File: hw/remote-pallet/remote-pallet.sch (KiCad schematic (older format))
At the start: 25 parts, among them J1 Power, M0 E-MATCH, M1 E-MATCH, M2 E-MATCH, M3 E-MATCH, M4 E-MATCH, M5 E-MATCH, M6 E-MATCH, M7 E-MATCH, Q1 EMatch Test, SW1 Power, SW2 Arm Hardware, U1 Photon Power, U2 PHOTON, U3 Armed Sense

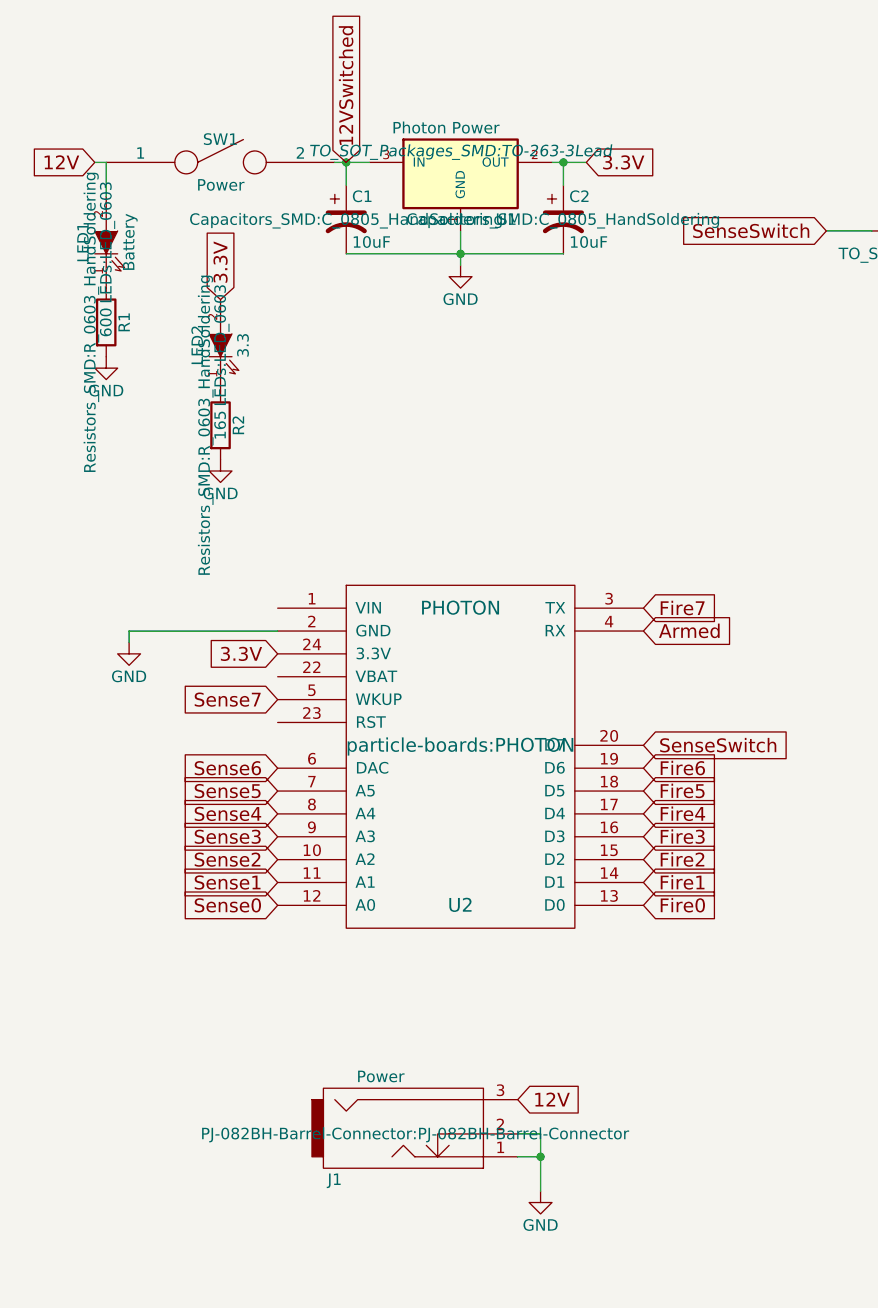
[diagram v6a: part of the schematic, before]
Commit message: updating pcb and adding part numbers for digikey
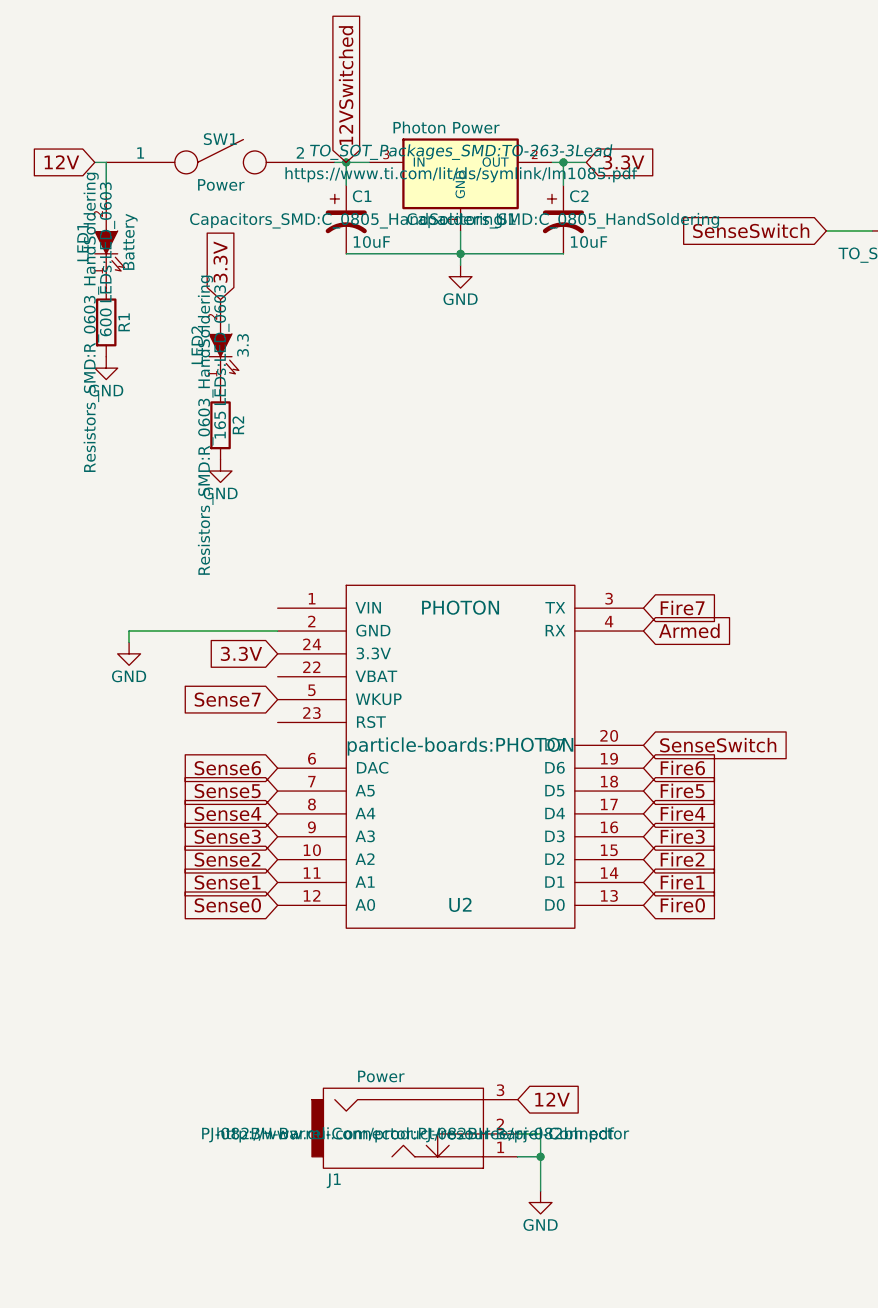
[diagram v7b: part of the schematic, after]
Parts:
- C1, C2: digikey part no (none) -> 511-1683-1-ND
- C3: digikey part no (none) -> 587-1290-1-ND
- C4: digikey part no (none) -> 490-5523-1-ND
- J1: digikey part no (none) -> CP-082BHCT-ND; mates with (none) -> CP3-002BH-ND
- LED1: digikey part no (none) -> 732-4978-1-ND
- LED2: digikey part no (none) -> 732-4981-1-ND
- LED3: digikey part no (none) -> 732-4971-1-ND
- M0, M1, M2, M3, M4, M5, M6, M7: digikey part no (none) -> ED2740-ND
- Q1: digikey part no (none) -> BSS84PH6433XTMA1CT-ND
- R1, R3: digikey part no (none) -> 311-600HCT-ND
- R2: digikey part no (none) -> 311-165HRCT-ND
- SW1, SW2: digikey part no (none) -> 360-3287-ND
- U1: digikey part no (none) -> LM1085ISX-3.3/NOPBCT-ND
- U3: digikey part no (none) -> TA48S033AF(T6L1Q)CT-ND
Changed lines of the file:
@@
 F 1 "Photon Power" H 2050 1200 50  0000 L CNN
 F 2 "TO_SOT_Packages_SMD:TO-263-3Lead" H 2350 1100 50  0000 C CIN
-F 3 "" H 2350 1000 50  0000 C CNN
+F 3 "https://www.ti.com/lit/ds/symlink/lm1085.pdf" H 2350 1000 50  0000 C CNN
+F 4 "LM1085ISX-3.3/NOPBCT-ND" H 2350 1000 60  0001 C CNN "digikey part no"
 	1    2350 1000
 	1    0    0    -1
@@
 F 2 "M2011LL1W01-switch:M2011LL1W01" H 9250 1250 50  0001 C CNN
 F 3 "" H 9250 1250 50  0000 C CNN
+F 4 "360-3287-ND" H 9250 1250 60  0001 C CNN "digikey part no"
 	1    9250 1250
 	1    0    0    -1
@@
 F 2 "TO_SOT_Packages_SMD:SOT-23" H 4550 1350 50  0000 C CNN
 F 3 "" H 4350 1250 50  0000 C CNN
+F 4 "BSS84PH6433XTMA1CT-ND" H 4350 1250 60  0001 C CNN "digikey part no"
 	1    4350 1250
 	1    0    0    1
@@
 F 2 "M2011LL1W01-switch:M2011LL1W01" H 1300 950 50  0001 C CNN
 F 3 "" H 1300 950 50  0000 C CNN
+F 4 "360-3287-ND" H 1300 950 60  0001 C CNN "digikey part no"
 	1    1300 950
 	1    0    0    -1
@@
 F 3 "" H 1850 1200 50  0000 C CNN
 F 4 "tantalum" H 1850 1200 60  0001 C CNN "type"
+F 5 "511-1683-1-ND" H 1850 1200 60  0001 C CNN "digikey part no"
 	1    1850 1200
 	1    0    0    -1
@@
 F 3 "" H 2800 1200 50  0000 C CNN
 F 4 "tantalum" H 2800 1200 60  0001 C CNN "type"
+F 5 "511-1683-1-ND" H 2800 1200 60  0001 C CNN "digikey part no"
 	1    2800 1200
 	1    0    0    -1
@@
 F 3 "" H 5700 1000 50  0000 C CNN
 F 4 "low-esr ceramic" H 5700 1000 60  0001 C CNN "type"
+F 5 "587-1290-1-ND" H 5700 1000 60  0001 C CNN "digikey part no"
 	1    5700 1000
 	1    0    0    -1
@@
 F 3 "" H 6750 1050 50  0000 C CNN
 F 4 "low-esr ceramic" H 6750 1050 60  0001 C CNN "type"
+F 5 "490-5523-1-ND" H 6750 1050 60  0001 C CNN "digikey part no"
 	1    6750 1050
 	1    0    0    -1
@@
 F 2 "Terminal_Blocks:TerminalBlock_Pheonix_PT-3.5mm_2pol" H 7050 2500 50  0001 C CNN
 F 3 "" H 7050 2500 50  0000 C CNN
+F 4 "ED2740-ND" H 7050 2500 60  0001 C CNN "digikey part no"
 	1    7050 2500
 	0    1    1    0
@@
 F 2 "Terminal_Blocks:TerminalBlock_Pheonix_PT-3.5mm_2pol" H 7050 3550 50  0001 C CNN
 F 3 "" H 7050 3550 50  0000 C CNN
+F 4 "ED2740-ND" H 7050 3550 60  0001 C CNN "digikey part no"
 	1    7050 3550
 	0    1    1    0
@@
 F 2 "Terminal_Blocks:TerminalBlock_Pheonix_PT-3.5mm_2pol" H 7050 4450 50  0001 C CNN
 F 3 "" H 7050 4450 50  0000 C CNN
+F 4 "ED2740-ND" H 7050 4450 60  0001 C CNN "digikey part no"
 	1    7050 4450
 	0    1    1    0
@@
 F 2 "Terminal_Blocks:TerminalBlock_Pheonix_PT-3.5mm_2pol" H 7050 5450 50  0001 C CNN
 F 3 "" H 7050 5450 50  0000 C CNN
+F 4 "ED2740-ND" H 7050 5450 60  0001 C CNN "digikey part no"
 	1    7050 5450
 	0    1    1    0
@@
 F 2 "Terminal_Blocks:TerminalBlock_Pheonix_PT-3.5mm_2pol" H 10050 2500 50  0001 C CNN
 F 3 "" H 10050 2500 50  0000 C CNN
+F 4 "ED2740-ND" H 10050 2500 60  0001 C CNN "digikey part no"
 	1    10050 2500
 	0    1    1    0
@@
 F 2 "Terminal_Blocks:TerminalBlock_Pheonix_PT-3.5mm_2pol" H 10050 3550 50  0001 C CNN
 F 3 "" H 10050 3550 50  0000 C CNN
+F 4 "ED2740-ND" H 10050 3550 60  0001 C CNN "digikey part no"
 	1    10050 3550
 	0    1    1    0
@@
 F 2 "Terminal_Blocks:TerminalBlock_Pheonix_PT-3.5mm_2pol" H 10050 4450 50  0001 C CNN
 F 3 "" H 10050 4450 50  0000 C CNN
+F 4 "ED2740-ND" H 10050 4450 60  0001 C CNN "digikey part no"
 	1    10050 4450
 	0    1    1    0
@@
 F 2 "Terminal_Blocks:TerminalBlock_Pheonix_PT-3.5mm_2pol" H 10050 5500 50  0001 C CNN
 F 3 "" H 10050 5500 50  0000 C CNN
+F 4 "ED2740-ND" H 10050 5500 60  0001 C CNN "digikey part no"
 	1    10050 5500
 	0    1    1    0
@@
 F 1 "Power" H 2000 5450 50  0000 C CNN
 F 2 "PJ-082BH-Barrel-Connector:PJ-082BH-Barrel-Connector" H 2150 5200 50  0000 C CNN
-F 3 "" H 2150 5200 50  0000 C CNN
+F 3 "http://www.cui.com/product/resource/pj-082bh.pdf" H 2150 5200 50  0000 C CNN
+F 4 "CP-082BHCT-ND" H 2150 5200 60  0001 C CNN "digikey part no"
+F 5 "CP3-002BH-ND" H 2150 5200 60  0001 C CNN "mates with"
 	1    2150 5200
 	1    0    0    -1
@@
 F 2 "TO_SOT_Packages_SMD:SOT-23-5" H 6250 850 50  0000 C CIN
 F 3 "http://ww1.microchip.com/downloads/en/DeviceDoc/MIC94310.pdf" H 6250 750 50  0000 C CNN
+F 4 "TA48S033AF(T6L1Q)CT-ND" H 6250 750 60  0001 C CNN "digikey part no"
 	1    6250 750
 	-1   0    0    -1
@@
 F 2 "LEDs:LED_0603" H 800 1300 50  0000 C CNN
 F 3 "" H 800 1300 50  0000 C CNN
+F 4 "732-4978-1-ND" H 800 1300 60  0001 C CNN "digikey part no"
 	1    800  1300
 	0    -1   -1   0
@@
 F 2 "LEDs:LED_0603" H 1300 1750 50  0000 C CNN
 F 3 "" H 1300 1750 50  0000 C CNN
+F 4 "732-4981-1-ND" H 1300 1750 60  0001 C CNN "digikey part no"
 	1    1300 1750
 	0    -1   -1   0
@@
 F 2 "LEDs:LED_0603" H 10400 1850 50  0000 C CNN
 F 3 "" H 10400 1850 50  0000 C CNN
+F 4 "732-4971-1-ND" H 10400 1850 60  0001 C CNN "digikey part no"
 	1    10400 1850
 	0    -1   -1   0
@@
 F 2 "Resistors_SMD:R_0603_HandSoldering" V 730 1650 50  0000 C CNN
 F 3 "" H 800 1650 50  0000 C CNN
+F 4 "311-600HCT-ND" V 800 1650 60  0001 C CNN "digikey part no"
 	1    800  1650
 	1    0    0    -1
@@
 F 2 "Resistors_SMD:R_0603_HandSoldering" V 10330 2200 50  0000 C CNN
 F 3 "" H 10400 2200 50  0000 C CNN
+F 4 "311-600HCT-ND" V 10400 2200 60  0001 C CNN "digikey part no"
 	1    10400 2200
 	1    0    0    -1
@@
 F 2 "Resistors_SMD:R_0603_HandSoldering" V 1230 2100 50  0000 C CNN
 F 3 "" H 1300 2100 50  0000 C CNN
+F 4 "311-165HRCT-ND" V 1300 2100 60  0001 C CNN "digikey part no"
 	1    1300 2100
 	1    0    0    -1

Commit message: updating schematic and PCB
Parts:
- added C5: 100pF, Capacitors_SMD:C_0805_HandSoldering, symbol C
- 3.3V1: renamed from LED2; value 3.3 -> Yellow
- Armed1: renamed from LED3; value Armed -> Green
- Battery1: renamed from LED1; value Battery -> Red
- C3: value 0.47uF -> 10uF
- Q1: symbol Q_PMOS_DGS -> Q_PMOS_GSD
- U3: digikey part no TA48S033AF(T6L1Q)CT-ND -> AP2202K-3.3TRG1DICT-ND
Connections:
- net 3.3V: now also Q1.2 (S); no longer Q1.3 (S)
- net Fire0: now also U2.16 (D3); no longer U2.13 (D0)
- net Fire1: now also U2.17 (D4); no longer U2.14 (D1)
- net Fire2: now also U2.18 (D5); no longer U2.15 (D2)
- net Fire3: now also U2.19 (D6); no longer U2.16 (D3)
- net Fire4: now also U2.15 (D2); no longer U2.17 (D4)
- net Fire5: now also U2.14 (D1); no longer U2.18 (D5)
- net Fire6: now also U2.13 (D0); no longer U2.19 (D6)
- net GND: now also C5.2
- net SenseSwitch: now also Q1.1 (G); no longer Q1.2 (G)
- net VCCsense: now also Q1.3 (D); no longer Q1.1 (D)
- net ematch-0/VCC: now also U3.3 (HEATSINK)
- net at U3.4 (NC): now also C5.1
